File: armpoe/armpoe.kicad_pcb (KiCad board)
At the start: 2 copper layers, 60 x 60 mm, 112 parts, among them J101 RJ45, Q101 Si4848DY, Q102 Si4848DY, Q103 Si4848DY, Q104 Si2325DS, T101 H2019, T102 HA3691-AL, U101 PM8803, U102 OPTO-TRANSISTOR, U103 TS431, U201 STM32F107XXX-LQFP64, U202 KSZ8041, U203 MCP1603, X202 CRYSTAL

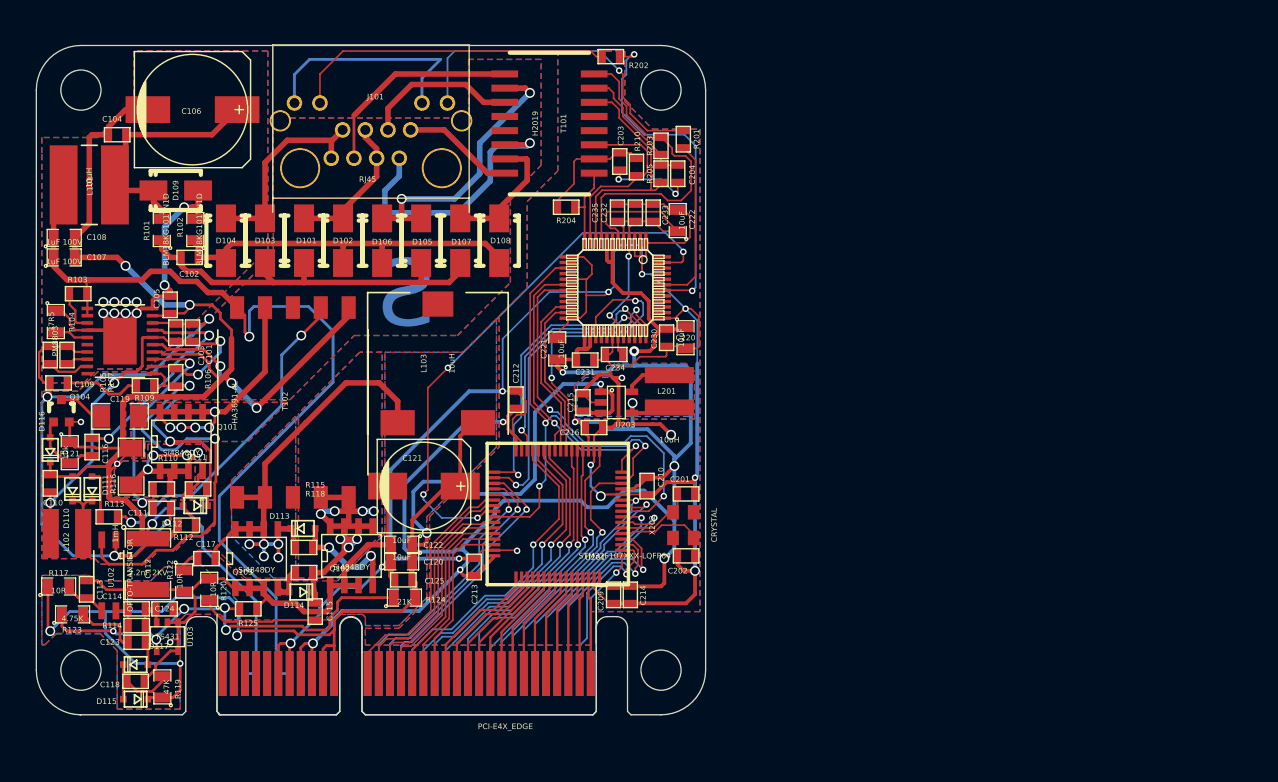
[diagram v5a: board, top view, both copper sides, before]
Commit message: most of the fixes form V1. looking to change pinout.
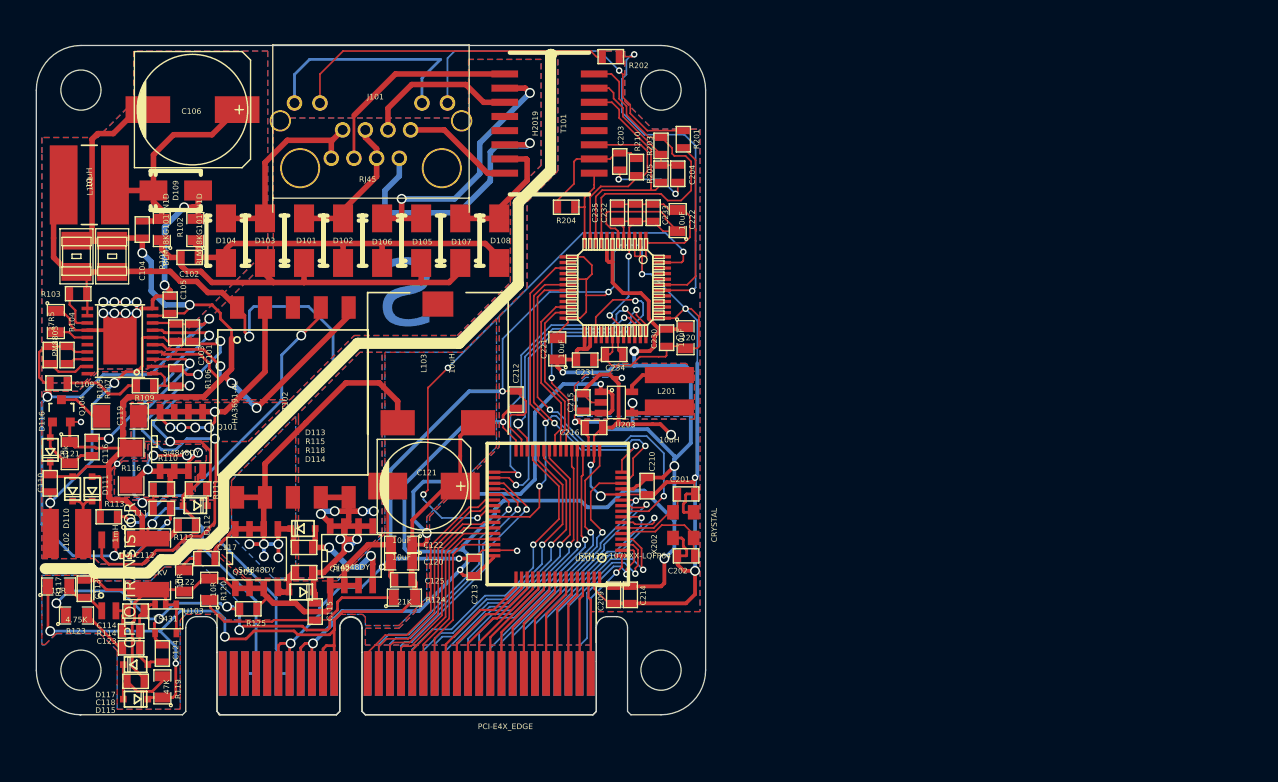
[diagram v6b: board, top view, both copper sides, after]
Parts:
- C107, C108: footprint SM0805 -> -C1210
- moved C104 8.79 mm to (189.5, 76.5), turned to 270 degrees
- moved C108 4.61 mm to (186.8, 78.9), turned to 90 degrees
- moved C124 4.00 mm to (191.3, 114.5), turned to 90 degrees
- moved U103 1.61 mm to (191.6, 111.4)
- moved C107 1.10 mm to (183.6, 78.9), turned to 90 degrees
- moved C123 0.71 mm to (188.5, 114.0)
- moved R114 0.71 mm to (188.5, 112.5)
- moved R123 0.36 mm to (183.6, 111.1)
- moved C114 0.22 mm to (188.9, 110.7)
- moved C113 0.21 mm to (184.3, 108.7)
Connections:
- X202 pad 3: (no net) -> GND
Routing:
- net GND: track 289.3 -> 299.3 mm, vias 17 -> 16
- net +5V: track 123.9 -> 115.9 mm
- net /MCU/Unisolated 48 -: track 141.4 -> 145.2 mm
- net N-0000051: track 40.2 -> 42.3 mm, vias 5 -> 4
- net N-0000052: track 5.74 -> 4.39 mm
- net /MCU/Unisolated 48 +: track 82.2 -> 81.2 mm
- net N-0000018: track 2.68 -> 3.23 mm
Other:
- net class Default: clearance 0.1778 -> 0.05
- rule trace_clearance: 0.1778 -> 0.05

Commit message: got everything rerouted, still haven't changed pinout. Still need to route int line.
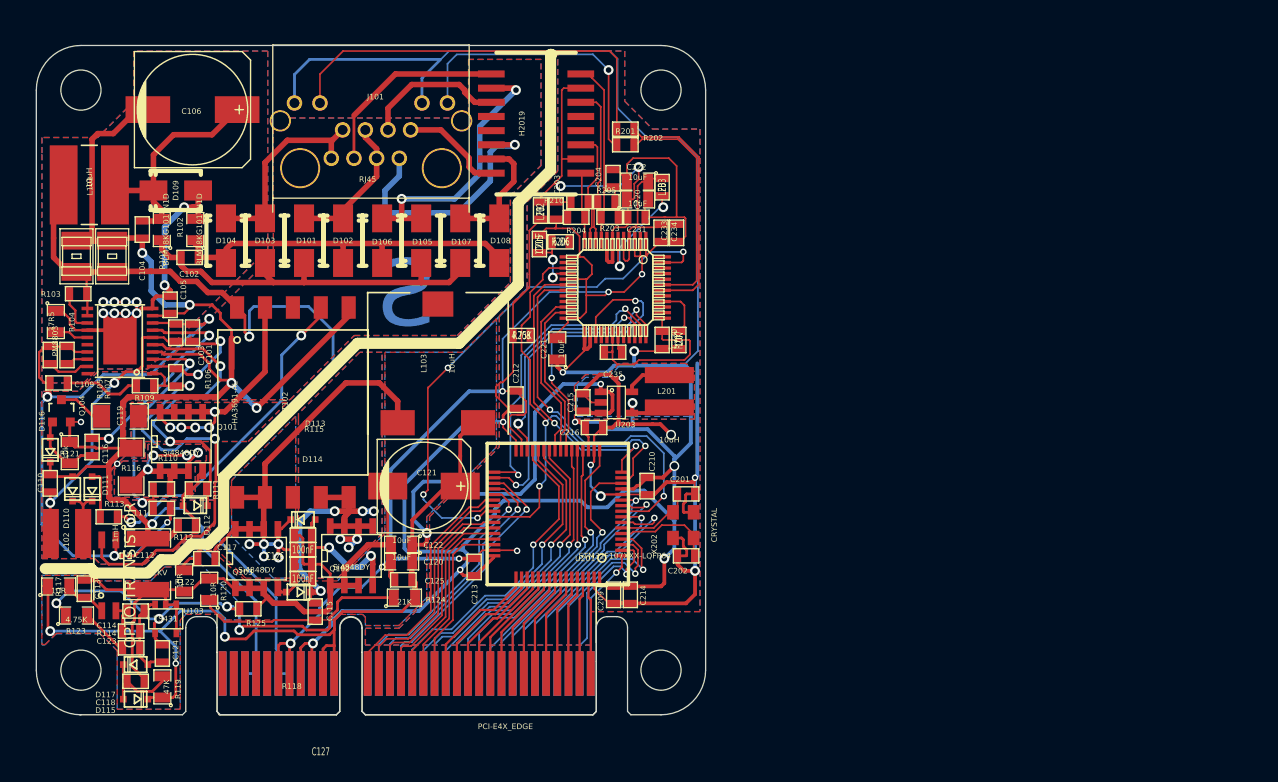
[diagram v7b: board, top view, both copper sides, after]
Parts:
- removed C232: 100nF, SM0603
- added C126: 100nF, SM0603, F.Cu at (203.9, 105.2)
- added C127: 100nF, SM0603, F.Cu at (203.9, 107.8)
- added C205: 100nF, SM0603, F.Cu at (225.1, 77.8)
- added L202: FB, SM0603, F.Cu at (225.2, 74.8)
- added L203: FB, SM0603, F.Cu at (236.1, 72.7)
- added R206: 6.8K, SM0603, F.Cu at (227.0, 77.6)
- added R207: 10K, SM0603, F.Cu at (237.6, 86.4)
- added R208: 4.75K, SM0603, F.Cu at (223.5, 86.0)
- R115, R118: value 5R6 -> 100K
- R125: value 6.78k -> 6.8K
- moved C231 13.6 mm to (233.8, 75.4)
- moved C220 13.1 mm to (233.9, 73.8), turned to 0 degrees
- moved C235 12.5 mm to (231.7, 87.5), turned to 180 degrees
- moved C234 11.7 mm to (236.0, 76.8), turned to 270 degrees
- moved R203 7.88 mm to (231.4, 75.4), turned to 180 degrees
- moved C203 7.20 mm to (226.6, 74.8)
- moved R202 6.63 mm to (232.8, 67.5)
- moved R210 5.97 mm to (228.7, 74.0), turned to 0 degrees
- moved C204 5.81 mm to (231.7, 71.9), turned to 270 degrees
- moved R205 5.50 mm to (231.1, 74.0), turned to 0 degrees
- moved R201 5.22 mm to (232.8, 68.9), turned to 180 degrees
- moved C222 5.02 mm to (233.9, 72.2), turned to 180 degrees
- moved C233 2.77 mm to (237.4, 76.8), turned to 270 degrees
- moved R204 1.27 mm to (228.4, 75.4)
- moved T101 1.20 mm to (224.8, 67.0)
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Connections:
- net N-0000022 renamed /activeGate1
- C115 pad 1: N-0000021 -> /conv_out_2
- C117 pad 1: N-0000058 (its old number) -> /conv_out_1
- C203 pad 1: /MCU/TXCT -> N-0000090
- C204 pad 2: /MCU/RXCT -> N-0000088
- C220 pad 1: +3.3V -> /MCU/RXCT
- C231 pad 1: +3.3V -> /MCU/RXCT
- C235 pad 1: +1.8V -> N-0000086
- D113 pad 2: N-0000058 (its old number) -> /conv_out_1
- D114 pad 1: N-0000061 -> /activeGate2
- D114 pad 2: N-0000021 -> /conv_out_2
- J101 pad 10: /MCU/3.3V -> +3.3V
- J101 pad 12: /MCU/3.3V -> +3.3V
- L103 pad 1: N-0000058 (its old number) -> /conv_out_1
- Q102 pad D: N-0000021 -> /conv_out_2
- Q103 pad D: N-0000058 (its old number) -> /conv_out_1
- Q103 pad G: N-0000061 -> /activeGate2
- R115 pad 1: N-0000058 (its old number) -> GND
- R118 pad 1: N-0000021 -> /activeGate2
- R118 pad 2: N-0000061 -> GND
- R203 pad 1: /MCU/RXCT -> N-0000088
- R204 pad 1: /MCU/TXCT -> N-0000090
- R205 pad 2: /MCU/RXCT -> N-0000088
- R210 pad 1: /MCU/TXCT -> N-0000090
- T101 pad 2: /MCU/TXCT -> /MCU/RXCT
- T102 pad 10: N-0000058 (its old number) -> /conv_out_1
- T102 pad 6: N-0000021 -> /conv_out_2
- T102 pad 7: N-0000021 -> /conv_out_2
- T102 pad 9: N-0000058 (its old number) -> /conv_out_1
- U202 pad 16: (no net) -> /MCU/ETH_REXT
- U202 pad 31: +1.8V -> N-0000086
- U202 pad 40: (no net) -> N-0000085
- U202 pad 6: +1.8V -> N-0000087
- U202 pad 7: +3.3V -> /MCU/RXCT
- U202 pad 8: +3.3V -> /MCU/RXCT
- X202 pad 3: GND -> (no net)
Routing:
- net +3.3V: track 174.3 -> 248.0 mm
- net /conv_out_1: track 0.00 -> 42.8 mm, vias 0 -> 5
- net N-0000058 (its old number): track 42.6 -> 0.00 mm, vias 5 -> 0
- net /conv_out_2: track 0.00 -> 30.5 mm, vias 0 -> 7
- net N-0000021: track 27.7 -> 0.00 mm, vias 7 -> 0
- net /MCU/RXCT: track 11.9 -> 35.4 mm, vias 0 -> 2
- net /MCU/3.3V: track 20.8 -> 0.00 mm
- net +1.8V: track 31.5 -> 16.0 mm, vias 2 -> 0
- net /MCU/RX-: track 28.8 -> 16.3 mm
- net /MCU/TXCT: track 10.8 -> 0.00 mm
- net N-0000087: track 0.00 -> 10.6 mm, vias 0 -> 2
- net N-0000070: track 30.8 -> 21.8 mm, vias 2 -> 0
- net /MCU/LED1: track 29.0 -> 36.8 mm
- net /MCU/RX+: track 21.5 -> 14.2 mm
- net /MCU/TX-: track 16.9 -> 10.5 mm
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- added copper zone on B.Cu, net /conv_out_1
- added copper zone on F.Cu, net /conv_out_1
- added copper zone on B.Cu, net N-000004
- added copper zone on F.Cu, net N-000004
- added copper zone on B.Cu, net N-000006
- added copper zone on F.Cu, net N-000006
- removed copper zone on B.Cu, net N-000001
- removed copper zone on F.Cu, net N-000001
- removed copper zone on B.Cu, net N-0000021
- removed copper zone on F.Cu, net N-0000021
- removed copper zone on B.Cu, net N-0000058 (its old number)
- removed copper zone on F.Cu, net N-0000058 (its old number)

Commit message: looks done, except the connector needs to be moved over (which will suck)
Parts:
- R116: value 0.6 -> 0.15
- X202: value CRYSTAL -> 25MHZ
- moved R110 10.7 mm to (195.0, 89.7), turned to 270 degrees
- moved L203 0.60 mm to (236.7, 72.7)
- moved C222 0.58 mm to (234.4, 71.9)
- moved C220 0.51 mm to (234.4, 73.7)
- moved C204 0.40 mm to (232.1, 71.9)
- moved C231 0.32 mm to (234.1, 75.3)
- moved L202 0.30 mm to (224.9, 74.8)
- moved C203 0.20 mm to (226.4, 74.8)
- moved C233 0.20 mm to (237.6, 76.8)
- moved R210 0.14 mm to (228.6, 73.9)
- moved C234 0.10 mm to (236.1, 76.8)
- moved R203 0.10 mm to (231.5, 75.4)
- moved R205 0.10 mm to (231.1, 73.9)
- moved R206 0.10 mm to (227.1, 77.6)
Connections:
- JP201 pad B32: /MCU/B32 -> (no net)
- U201 pad 62: /MCU/B32 -> /MCU/ETH_INT
- U202 pad 32: (no net) -> /MCU/ETH_INT
- X202 pad 3: (no net) -> GND
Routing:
- net /MCU/ETH_INT: track 0.00 -> 42.1 mm, vias 0 -> 2
- net N-000001: track 16.2 -> 26.5 mm, vias 4 -> 5
- net /MCU/B32: track 8.63 -> 0.00 mm
- net /PM8803_5V_REG: track 10.9 -> 13.2 mm
- net /MCU/Unisolated 48 -: track 148.6 -> 146.9 mm, vias 7 -> 6
- net /MCU/RXCT: track 35.4 -> 33.8 mm
- net GND: track 297.2 -> 295.8 mm
- net +5V: track 115.9 -> 114.7 mm
- net +3.3V: track 248.0 -> 249.2 mm
- net /MCU/RX-: track 16.3 -> 17.1 mm
- net /primary low: track 25.8 -> 26.4 mm
- net N-0000090: track 10.6 -> 11.2 mm
- net /ARTN: track 60.9 -> 61.5 mm
- added copper zone on B.Cu, net /conv_out_2
- added copper zone on F.Cu, net /conv_out_2
- removed copper zone on B.Cu, net N-000006
- removed copper zone on F.Cu, net N-000006
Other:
- net class Default: clearance 0.05 -> 0.1524
- net class smallest allowed: clearance 0.1778 -> 0.1524
- rule trace_clearance: 0.05 -> 0.1524
- board text added: "smg.codewarp.org"
- board text removed: "smg.ideacraft.org"
